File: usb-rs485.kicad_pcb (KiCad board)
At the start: 2 copper layers, 14.4 x 24.7 mm, 37 parts, among them IC1 THVD2450VDRCR, J1 USB4110GFA, U1 TPS63070, U12 DF52-4S-0.8H(21), U9 CP2102N-A02-GQFN24R

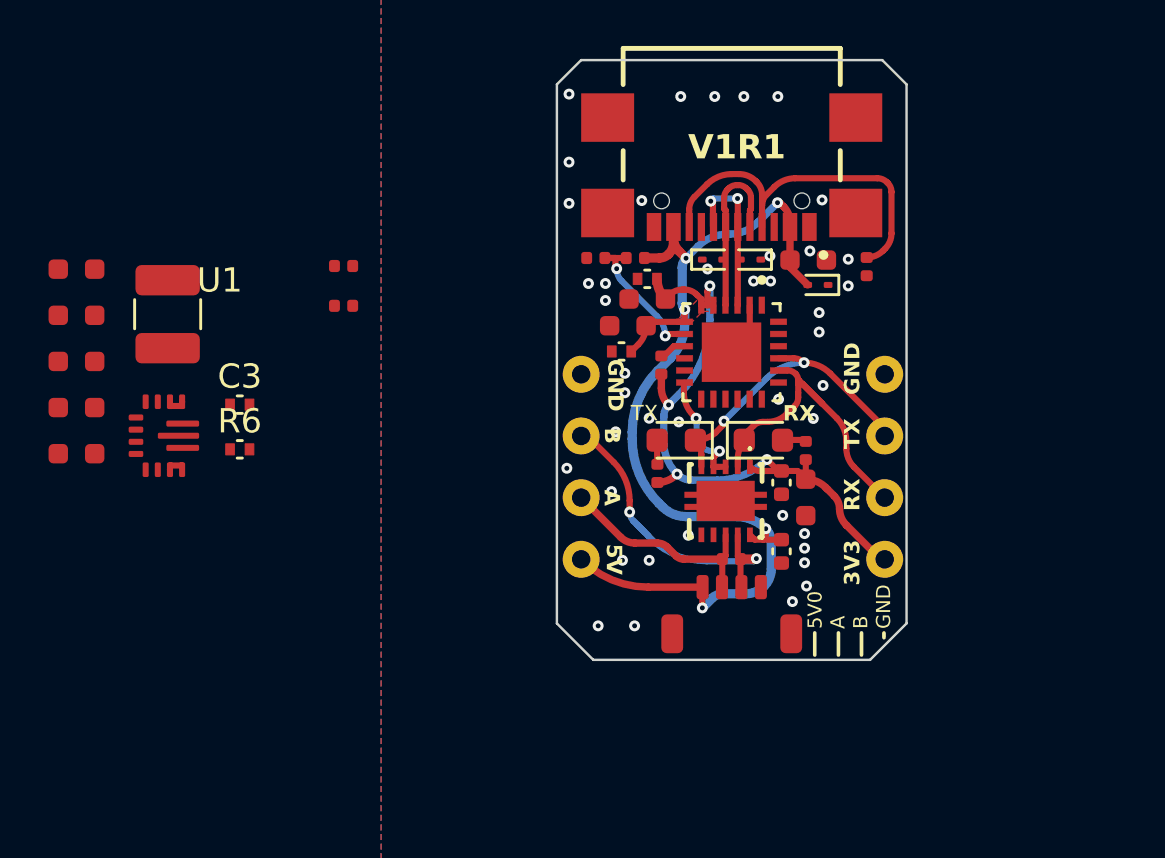
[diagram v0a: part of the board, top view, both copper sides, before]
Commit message: wiring in boost to 6V
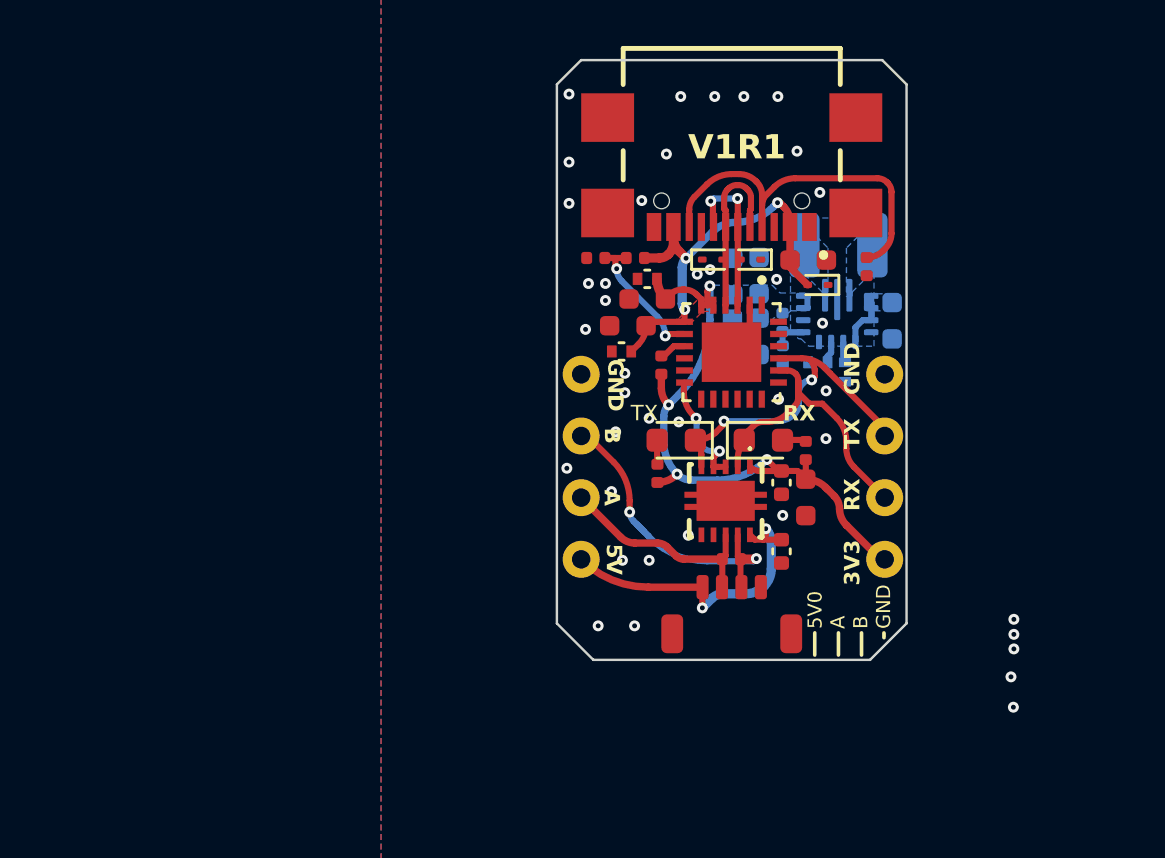
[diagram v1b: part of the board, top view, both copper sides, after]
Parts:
- C10, C11, C2, C3, C6, C7, L1, R4, R5, R6, U1: moved to B.Cu
- moved C2 33.7 mm to (149.7, 102.0), turned to -90 degrees
- moved C10 28.6 mm to (144.2, 100.1), turned to 90 degrees
- moved U1 28.2 mm to (147.5, 101.7), turned to 90 degrees
- moved C7 28.1 mm to (144.2, 102.6), turned to -90 degrees
- moved C11 28.0 mm to (143.2, 100.2), turned to 90 degrees
- moved L1 27.8 mm to (147.5, 98.9), turned to 180 degrees
- moved C6 27.0 mm to (143.1, 102.7), turned to -90 degrees
- moved R6 25.1 mm to (147.8, 104.1), turned to 90 degrees
- moved C3 23.9 mm to (146.7, 103.7), turned to 180 degrees
- moved R4 18.2 mm to (145.2, 102.0), turned to -90 degrees
- moved R5 18.2 mm to (145.2, 103.4), turned to -90 degrees
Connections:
- net Net-(U1-L1) renamed /PSU_TPS63070RNMR/L1
- net Net-(U1-L2) renamed /PSU_TPS63070RNMR/L2
- C10 pad 1: +3V3 -> /6V0
- C11 pad 1: +3V3 -> /6V0
- C2 pad 1: /V_GATEDRIVE -> /VUSB
- C6 pad 1: +3V3 -> /6V0
- C7 pad 1: +3V3 -> /6V0
- R4 pad 1: +3V3 -> /6V0
- R6 pad 1: +3V3 -> /6V0
- U1 pad 1: /V_GATEDRIVE -> /VUSB
- U1 pad 12,13: /V_GATEDRIVE -> /VUSB
- U1 pad 14: /V_GATEDRIVE -> /VUSB
- U1 pad 7,8: +3V3 -> /6V0
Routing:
- net /VUSB: track 44.6 -> 33.4 mm
- net /TX: track 12.7 -> 14.2 mm
- net /PSU_TPS63070RNMR/FB: track 0.00 -> 1.43 mm
- net Net-(U1-VAUX): track 0.00 -> 0.90 mm
- net Net-(U1-PG): track 0.00 -> 0.86 mm
- net /RX: track 13.5 -> 12.7 mm
- net GND: vias 42 -> 40
- added copper zone on B.Cu, net +3V3
- added copper zone on B.Cu, net /PSU_TPS63070RNMR/L1
- added copper zone on B.Cu, net /PSU_TPS63070RNMR/L2
- added copper zone on B.Cu, net /VUSB
- added copper zone on In1.Cu, net GND
- added copper zone on In2.Cu, net GND
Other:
- copper layers 2 -> 4

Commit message: moved it elsewhere but MEH
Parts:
- moved R6 14.9 mm to (139.4, 91.7), turned to 0 degrees
- moved C2 14.5 mm to (137.9, 93.5), turned to 90 degrees
- moved C3 13.2 mm to (141.0, 91.8), turned to 0 degrees
- moved R5 11.7 mm to (142.4, 92.1), turned to 90 degrees
- moved U1 10.8 mm to (140.2, 93.7), turned to -90 degrees
- moved C6 9.97 mm to (144.5, 92.8), turned to 90 degrees
- moved C7 9.83 mm to (143.4, 92.8), turned to 90 degrees
- moved R4 9.07 mm to (142.4, 93.4), turned to 90 degrees
- moved L1 7.72 mm to (140.1, 96.6), turned to 0 degrees
- moved C11 5.05 mm to (144.5, 95.3), turned to -90 degrees
- moved C10 4.86 mm to (143.4, 95.3), turned to -90 degrees
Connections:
- U12 pad 1: /VUSB -> /6V0
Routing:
- net /VUSB: track 33.4 -> 29.9 mm
- net /CP2102N/D+: track 6.67 -> 7.72 mm
- net GND: vias 40 -> 48
- added copper zone on B.Cu, net /6V0
- removed copper zone on B.Cu, net +3V3

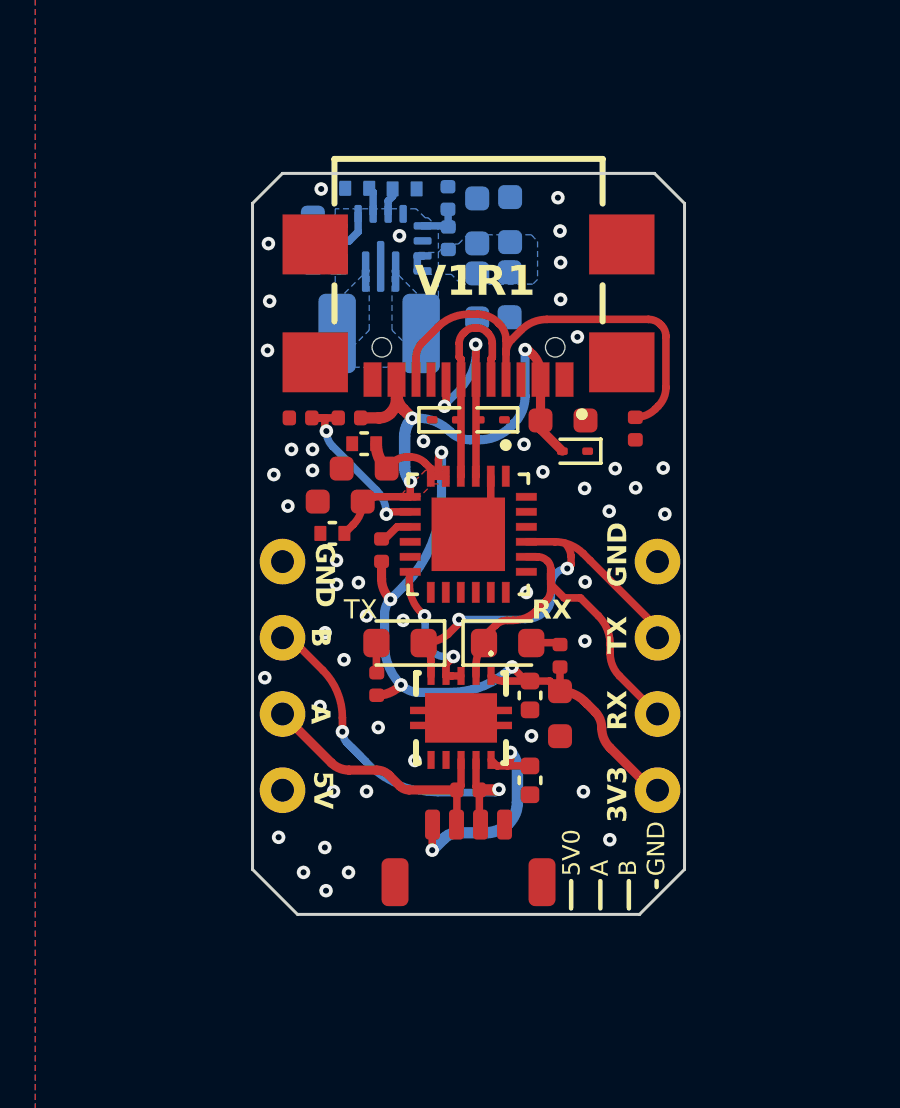
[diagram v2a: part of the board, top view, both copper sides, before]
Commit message: routed best placement. Has 6V on the output and on a final header hole for max conveniences
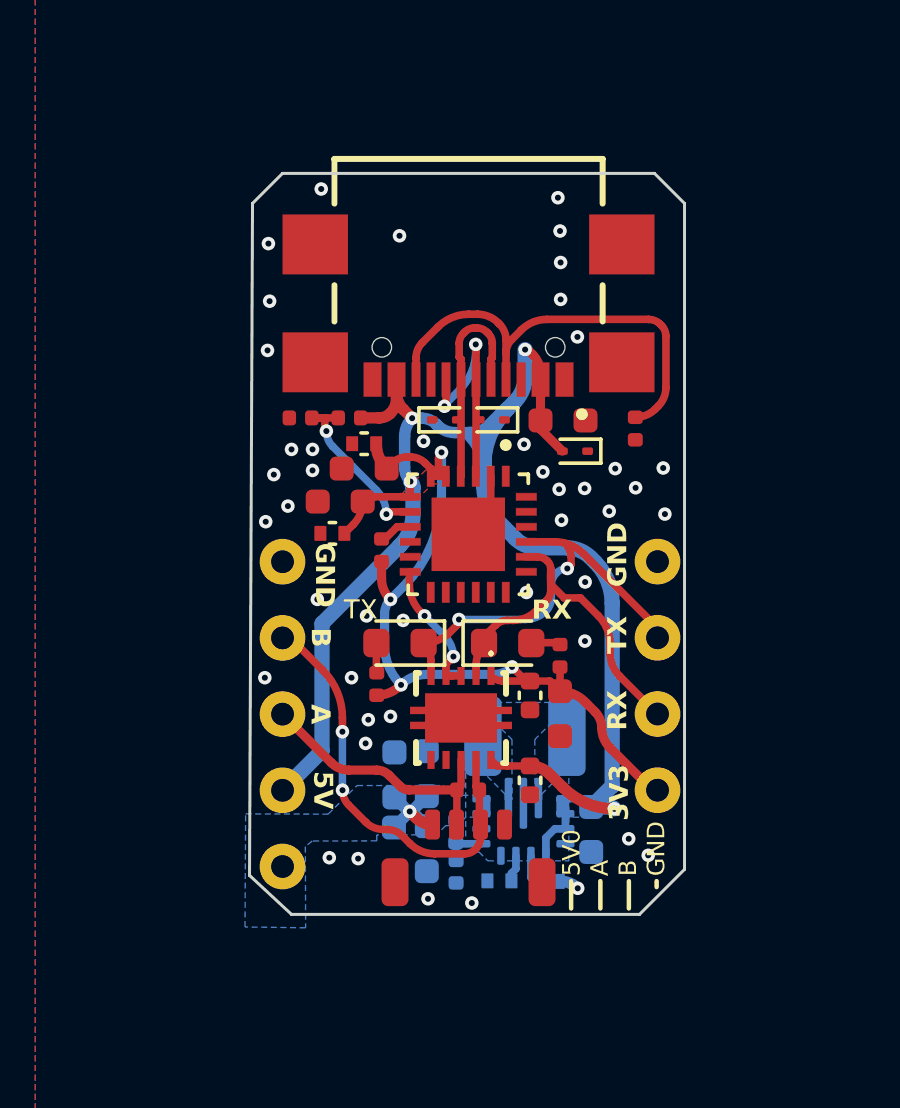
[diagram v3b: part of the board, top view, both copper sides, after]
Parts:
- J2: footprint usb-rs485:ThruHoleBreadboardX4 -> usb-rs485:ThruHoleBreadboardX5
- moved R6 24.0 mm to (145.7, 114.8), turned to 180 degrees
- moved C3 23.3 mm to (144.1, 114.8), turned to 180 degrees
- moved R5 22.5 mm to (142.7, 114.5), turned to -90 degrees
- moved C2 21.7 mm to (147.2, 113.1), turned to -90 degrees
- moved C6 21.4 mm to (140.6, 113.8), turned to -90 degrees
- moved C7 21.0 mm to (141.7, 113.8), turned to -90 degrees
- moved R4 19.8 mm to (142.7, 113.2), turned to -90 degrees
- moved U1 19.7 mm to (144.9, 112.8), turned to 90 degrees
- moved C11 16.5 mm to (140.6, 111.3), turned to 90 degrees
- moved C10 16.0 mm to (141.7, 111.2), turned to 90 degrees
- moved L1 14.3 mm to (145.0, 110.0), turned to 180 degrees
- moved J2 2.54 mm to (136.9, 110.5)
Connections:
- J2 pad 1: /VUSB -> /6V0
- J2 pad 2: /RS485 Transceiver/RS1_A -> /VUSB
- J2 pad 3: /RS485 Transceiver/RS1_B -> /RS485 Transceiver/RS1_A
- J2 pad 4: GND -> /RS485 Transceiver/RS1_B
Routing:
- net /VUSB: track 29.9 -> 59.3 mm, vias 5 -> 4
- net /6V0: track 0.00 -> 15.1 mm, vias 0 -> 2
- net GND: vias 48 -> 44
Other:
- board size 14.4 x 24.7 mm -> 14.5 x 24.7 mm

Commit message: resistors dialed in
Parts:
- R4: value 470k -> 365k
- R5: value 150k -> 47k
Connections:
- net /6V0 renamed /7V0
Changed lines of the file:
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@@
   (net 34 "/PSU_TPS63070RNMR/FB")
   (net 35 "Net-(U1-PG)")
-  (net 36 "/6V0")
+  (net 36 "/7V0")
   (footprint "usb-rs485:LED_0603_1608Metric" (layer "F.Cu")
     (at 144.4225 106.895)
@@
       (stroke (width 0.05) (type default)) (fill none) (layer "F.CrtYd"))
     (pad "1" smd roundrect (at -1.2 0 180) (size 0.5 1) (layers "F.Cu" "F.Paste" "F.Mask") (roundrect_rratio 0.25)
-      (net 36 "/6V0") (pinfunction "1") (pintype "input") (thermal_bridge_angle 45))
+      (net 36 "/7V0") (pinfunction "1") (pintype "input") (thermal_bridge_angle 45))
     (pad "2" smd roundrect (at -0.4 0 180) (size 0.5 1) (layers "F.Cu" "F.Paste" "F.Mask") (roundrect_rratio 0.25)
       (net 17 "/RS485 Transceiver/RS1_A") (pinfunction "2") (pintype "input") (thermal_bridge_angle 45))
@@
       (stroke (width 0.05) (type default)) (fill none) (layer "F.CrtYd"))
     (pad "1" thru_hole circle (at -3.81 0 90) (size 1.524 1.524) (drill 0.762) (layers "*.Cu" "*.Mask")
-      (net 36 "/6V0") (pinfunction "1") (pintype "input"))
+      (net 36 "/7V0") (pinfunction "1") (pintype "input"))
     (pad "2" thru_hole circle (at -1.27 0 90) (size 1.524 1.524) (drill 0.762) (layers "*.Cu" "*.Mask")
       (net 16 "/VUSB") (pinfunction "2") (pintype "input"))
@@
       (net 2 "GND") (pinfunction "FB2") (pintype "input") (solder_mask_margin 0.0508) (thermal_bridge_angle 45))
     (pad "7,8" smd custom (at 0.25 -1.4) (size 0.25 0.25) (layers "B.Cu" "B.Paste" "B.Mask")
-      (net 36 "/6V0") (pinfunction "VOUT") (pintype "input") (solder_mask_margin 0.0508)
+      (net 36 "/7V0") (pinfunction "VOUT") (pintype "input") (solder_mask_margin 0.0508)
       (options (clearance outline) (anchor circle))
       (primitives
@@
       (stroke (width 0.1) (type solid)) (layer "B.Fab"))
     (pad "1" smd roundrect (at -0.75 0 270) (size 0.8 0.8) (layers "B.Cu" "B.Paste" "B.Mask") (roundrect_rratio 0.25)
-      (net 36 "/6V0") (pintype "passive") (solder_mask_margin 0.0508))
+      (net 36 "/7V0") (pintype "passive") (solder_mask_margin 0.0508))
     (pad "2" smd roundrect (at 0.75 0 270) (size 0.8 0.8) (layers "B.Cu" "B.Paste" "B.Mask") (roundrect_rratio 0.25)
       (net 2 "GND") (pintype "passive") (solder_mask_margin 0.0508))
@@
         (effects (font (size 1 1) (thickness 0.15)) (justify mirror))
     )
-    (fp_text value "150k" (at 0 -1.17 90) (layer "B.Fab") hide
+    (fp_text value "47k" (at 0 -1.17 90) (layer "B.Fab") hide
         (effects (font (size 1 1) (thickness 0.15)) (justify mirror))
     )
@@
       (stroke (width 0.1) (type solid)) (layer "B.Fab"))
     (pad "1" smd roundrect (at -0.75 0 270) (size 0.8 0.8) (layers "B.Cu" "B.Paste" "B.Mask") (roundrect_rratio 0.25)
-      (net 36 "/6V0") (pintype "passive") (solder_mask_margin 0.0508))
+      (net 36 "/7V0") (pintype "passive") (solder_mask_margin 0.0508))
     (pad "2" smd roundrect (at 0.75 0 270) (size 0.8 0.8) (layers "B.Cu" "B.Paste" "B.Mask") (roundrect_rratio 0.25)
       (net 2 "GND") (pintype "passive") (solder_mask_margin 0.0508))
@@
       (stroke (width 0.1) (type solid)) (layer "B.Fab"))
     (pad "1" smd roundrect (at -0.75 0 90) (size 0.8 0.8) (layers "B.Cu" "B.Paste" "B.Mask") (roundrect_rratio 0.25)
-      (net 36 "/6V0") (pintype "passive") (solder_mask_margin 0.0508))
+      (net 36 "/7V0") (pintype "passive") (solder_mask_margin 0.0508))
     (pad "2" smd roundrect (at 0.75 0 90) (size 0.8 0.8) (layers "B.Cu" "B.Paste" "B.Mask") (roundrect_rratio 0.25)
       (net 2 "GND") (pintype "passive") (solder_mask_margin 0.0508))
@@
       (stroke (width 0.1) (type solid)) (layer "B.Fab"))
     (pad "1" smd roundrect (at -0.75 0 90) (size 0.8 0.8) (layers "B.Cu" "B.Paste" "B.Mask") (roundrect_rratio 0.25)
-      (net 36 "/6V0") (pintype "passive") (solder_mask_margin 0.0508))
+      (net 36 "/7V0") (pintype "passive") (solder_mask_margin 0.0508))
     (pad "2" smd roundrect (at 0.75 0 90) (size 0.8 0.8) (layers "B.Cu" "B.Paste" "B.Mask") (roundrect_rratio 0.25)
       (net 2 "GND") (pintype "passive") (solder_mask_margin 0.0508))
@@
       (stroke (width 0.1) (type solid)) (layer "B.Fab"))
     (pad "1" smd roundrect (at -0.4 0 180) (size 0.4 0.5) (layers "B.Cu" "B.Paste" "B.Mask") (roundrect_rratio 0.0625)
-      (net 36 "/6V0") (pintype "passive") (solder_mask_margin 0.0508))
+      (net 36 "/7V0") (pintype "passive") (solder_mask_margin 0.0508))
     (pad "2" smd roundrect (at 0.4 0 180) (size 0.4 0.5) (layers "B.Cu" "B.Paste" "B.Mask") (roundrect_rratio 0.0625)
       (net 35 "Net-(U1-PG)") (pintype "passive") (solder_mask_margin 0.0508))
@@
         (effects (font (size 1 1) (thickness 0.15)) (justify mirror))
     )
-    (fp_text value "470k" (at 0 -1.17 90) (layer "B.Fab") hide
+    (fp_text value "365k" (at 0 -1.17 90) (layer "B.Fab") hide
         (effects (font (size 1 1) (thickness 0.15)) (justify mirror))
     )
@@
       (stroke (width 0.1) (type solid)) (layer "B.Fab"))
     (pad "1" smd roundrect (at -0.375 0 270) (size 0.45 0.5) (layers "B.Cu" "B.Paste" "B.Mask") (roundrect_rratio 0.25)
-      (net 36 "/6V0") (pintype "passive") (solder_mask_margin 0.0508))
+      (net 36 "/7V0") (pintype "passive") (solder_mask_margin 0.0508))
     (pad "2" smd roundrect (at 0.375 0 270) (size 0.45 0.5) (layers "B.Cu" "B.Paste" "B.Mask") (roundrect_rratio 0.25)
       (net 34 "/PSU_TPS63070RNMR/FB") (pintype "passive") (solder_mask_margin 0.0508))
@@
     )
   )
-  (zone (net 36) (net_name "/6V0") (layer "B.Cu") (hatch edge 0.5)
+  (zone (net 36) (net_name "/7V0") (layer "B.Cu") (hatch edge 0.5)
     (priority 2)
     (connect_pads yes (clearance 0.1))
